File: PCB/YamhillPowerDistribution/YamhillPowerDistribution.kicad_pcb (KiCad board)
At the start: 2 copper layers, 50 x 50 mm, 56 parts, among them J1 CUI PJ-202AH, J10 12VDC, J11 12VDC, J12 12VDC, J13 12VDC, J14 12VDC, J15 12VDC, J16 12VDC, J17 12VDC, J18 3.3VDC, J19 3.3VDC, J2 5VDC, J20 3.3VDC, J21 3.3VDC, J22 3.3VDC, J23 3.3VDC, J24 3.3VDC, J25 3.3VDC, J26 12VDC, J27 12VDC, J28 12VDC, J29 12VDC, J3 5VDC, J30 12VDC, J31 12VDC, J32 12VDC, J33 12VDC, J34 12VDC, J35 12VDC, J4 5VDC, J5 5VDC, J6 5VDC, J7 5VDC, J8 5VDC, J9 5VDC, U1 L78M05CDT-TR, U2 AP2213-3.3

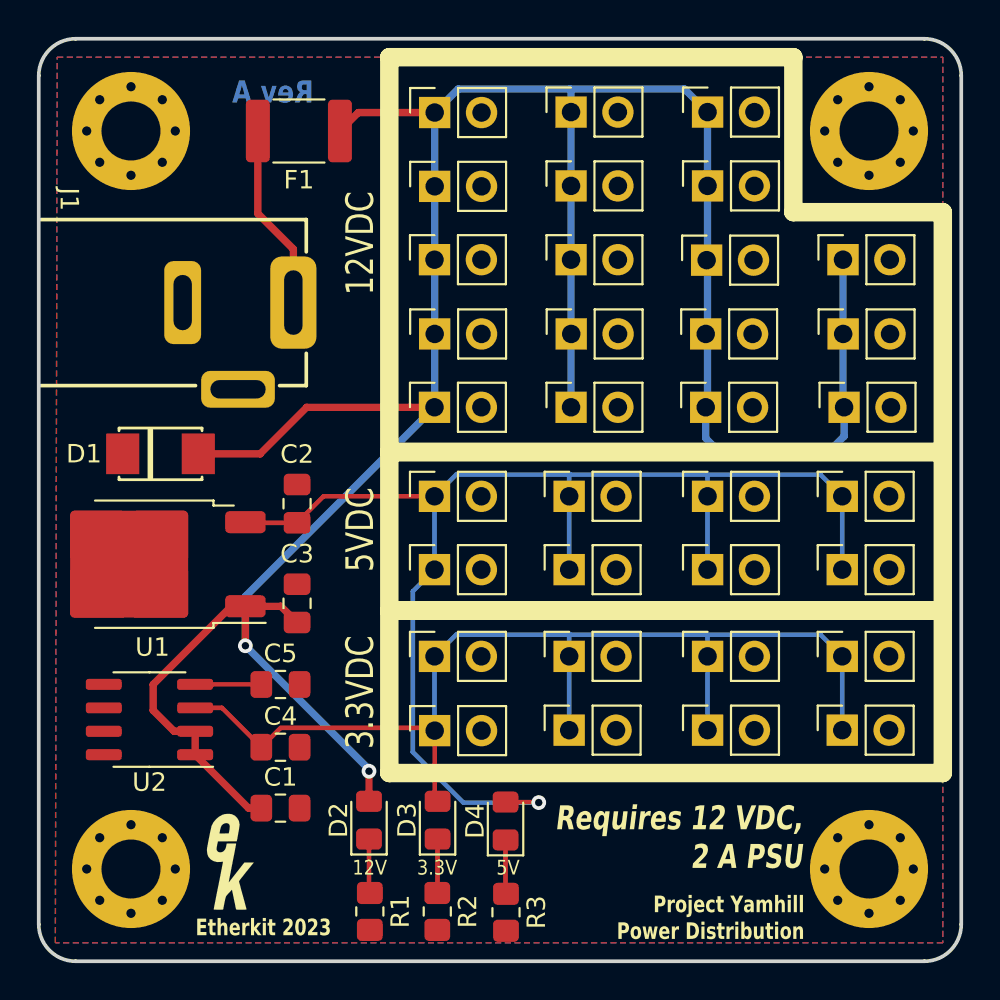
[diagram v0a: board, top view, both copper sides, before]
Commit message: Fix PCB template problems
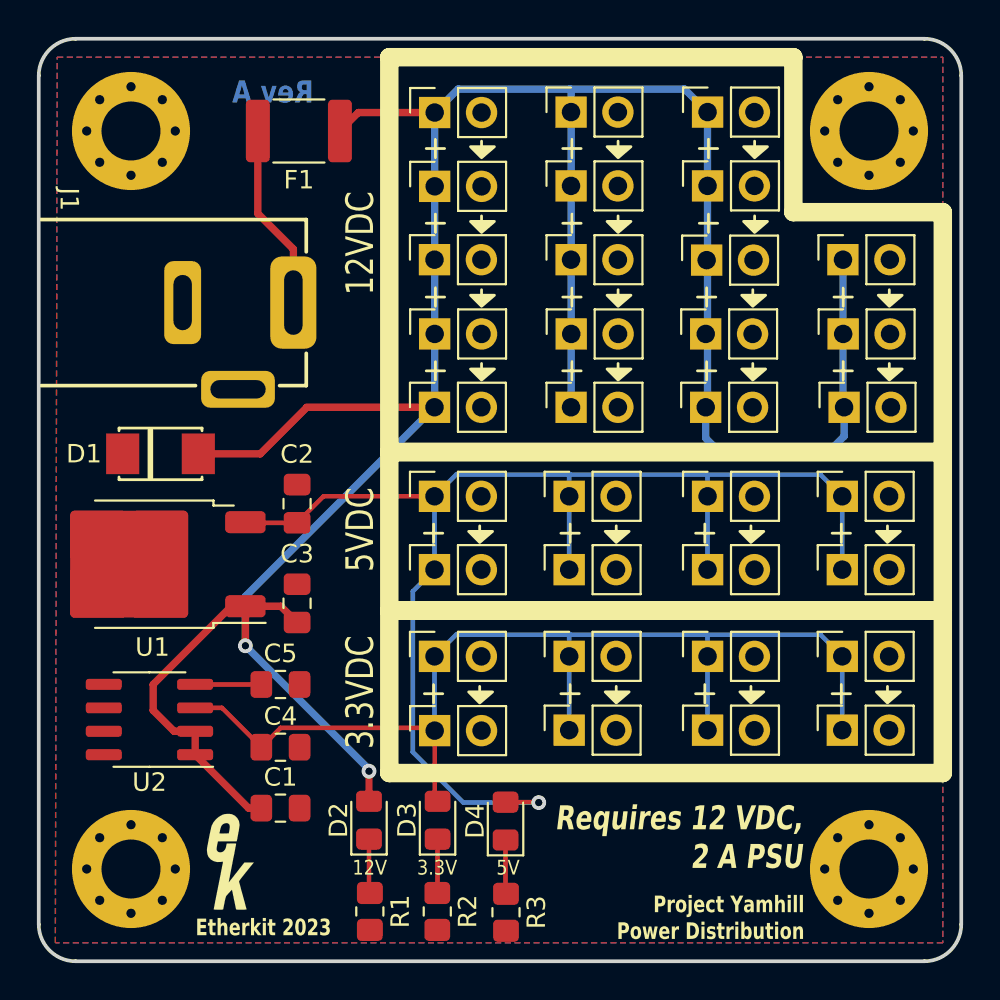
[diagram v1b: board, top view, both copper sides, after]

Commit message: Update all PCBs for first tranche order
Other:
- board text added: "Etherkit 2024"
- board text removed: "Etherkit 2023"

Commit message: Second tranche of PCBs
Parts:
- removed C5: 100p, Capacitor_SMD:C_0805_2012Metric_Pad1.18x1.45mm_HandSolder
- removed G***: LOGO, EtherkitKicadLibrary:OSHWLogo4mm
- removed Ref**: Val**, EtherkitKicadLibrary:EtherkitLogoSmall
- C1: value 33n -> 330n
- C3: value 1u -> 330n
- C4: value 2.2u -> 100n
- U1: value L78M05CDT-TR -> UA78M05IKVURG3
- U2: value AP2213-3.3 -> UA78M33CKVURG3; footprint Package_SO:SOIC-8_3.9x4.9mm_P1.27mm -> Package_TO_SOT_SMD:TO-252-2
- moved C4 2.85 mm to (114.0, 85.7), turned to 90 degrees
- moved C1 1.16 mm to (114.0, 91.0), turned to -90 degrees
- moved R1 0.60 mm to (117.9, 97.9)
- moved R2 0.60 mm to (121.6, 97.9)
- moved R3 0.56 mm to (125.3, 97.9)
- moved U2 0.38 mm to (106.1, 87.3)
- turned D1 to 90 degrees
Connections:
- U2 pad 2: Net-(D1-K) -> GND
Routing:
- net Net-(D1-K): track 154.6 -> 144.2 mm
- net Net-(D4-A): track 72.4 -> 76.9 mm
- net Net-(U2-BP): track 3.59 -> 0.00 mm
- net Net-(D3-K): track 2.93 -> 3.53 mm
- net Net-(D2-K): track 2.94 -> 3.52 mm
- net Net-(D4-K): track 2.93 -> 3.49 mm
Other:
- board text added: "Rev B"
- board text removed: "Rev A"
